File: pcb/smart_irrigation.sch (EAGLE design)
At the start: 24 parts, among them IC1 7805DT, IC2 7833DT, IC3 TMP36, J1 1X2-3.5MM, Q2 32.768

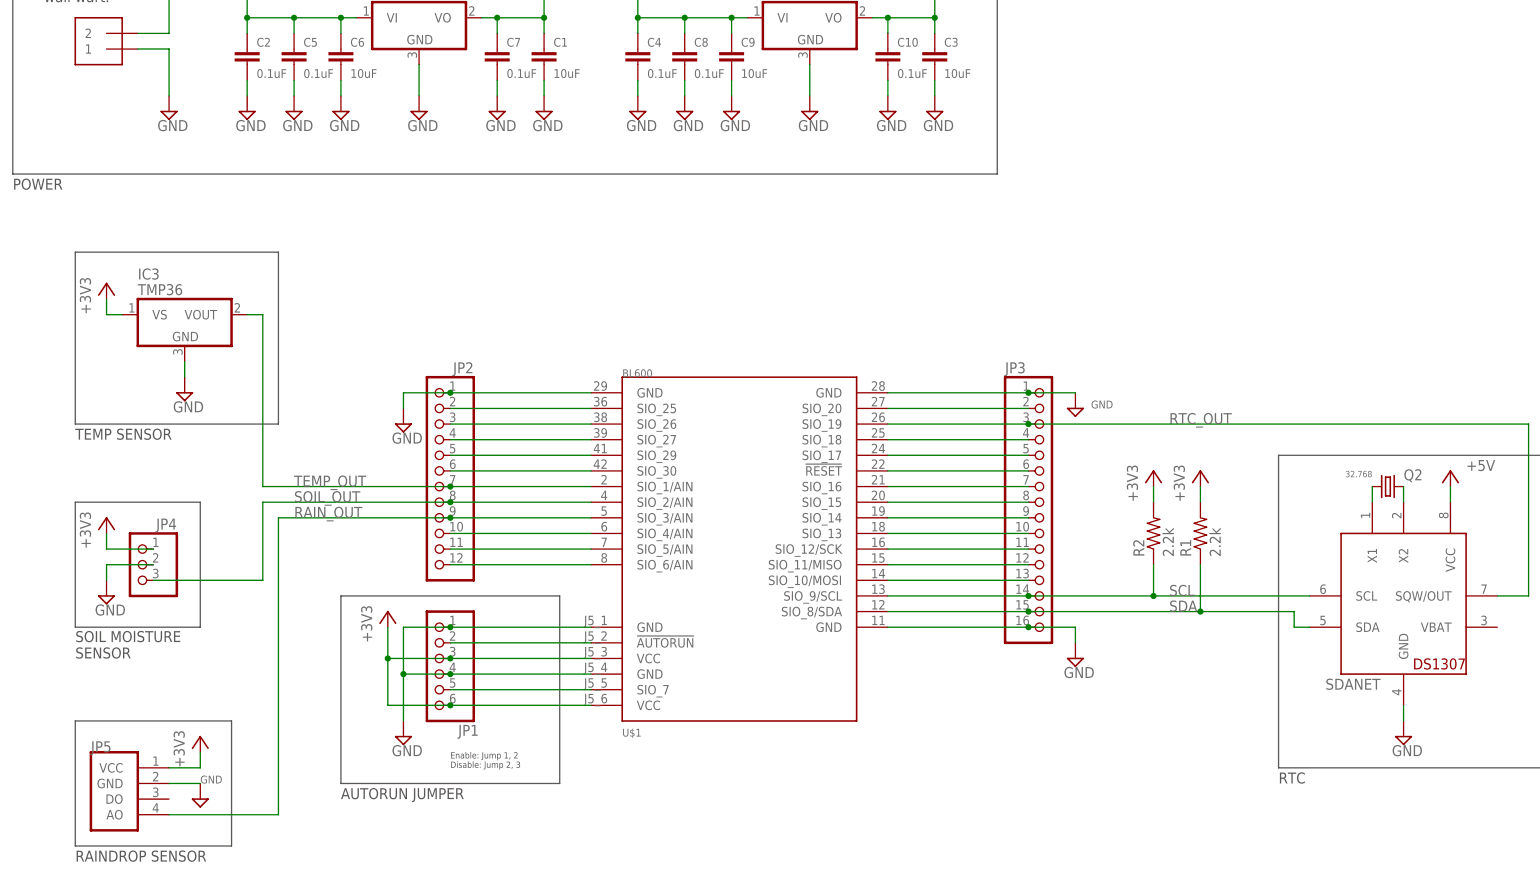
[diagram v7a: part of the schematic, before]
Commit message: PCB: Add caps across BL600 power input
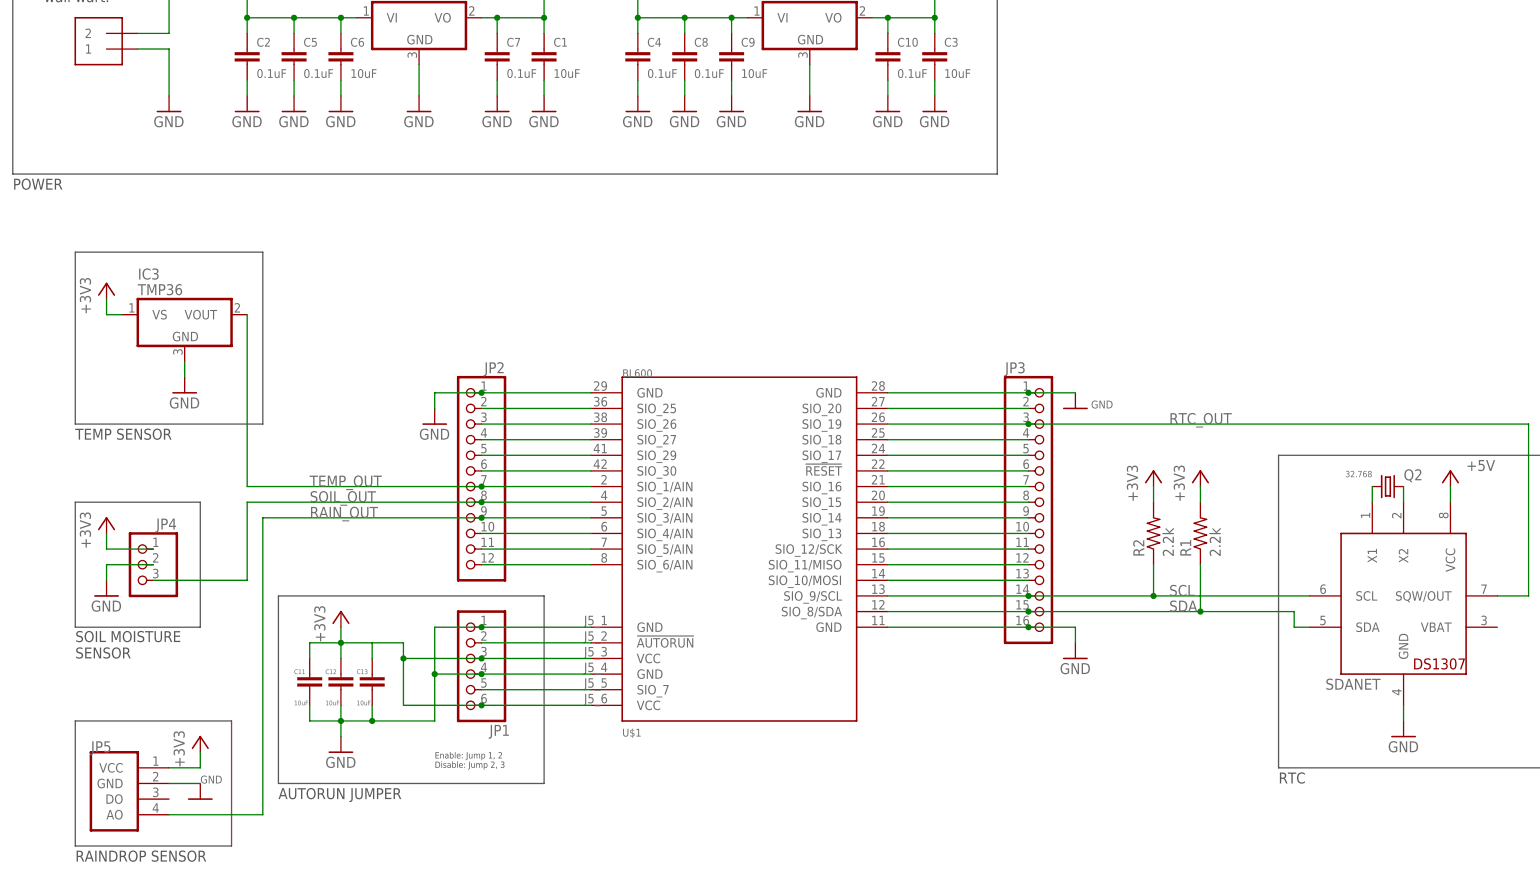
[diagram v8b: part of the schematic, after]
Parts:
- added C11, C12, C13: 10uF, rcl:C-EUC0805
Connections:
- net +3V3: now also C11.1, C12.1, C13.1
- net GND: now also C11.2, C12.2, C13.2
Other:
- moved on the sheet: JP1, JP2
